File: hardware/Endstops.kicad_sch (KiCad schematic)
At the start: 47 parts

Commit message: Convert SCH files to latest version. Fix DRC Warnings in PrntrBoard.
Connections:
- net ~ALARM1 renamed ~{ALARM1}
- net ~ST1_ALARM renamed ~{ST1_ALARM}
- net ~ST2_ALARM renamed ~{ST2_ALARM}
- net ~ST3_ALARM renamed ~{ST3_ALARM}
- net ~ST4_ALARM renamed ~{ST4_ALARM}
- net ~ST5_ALARM renamed ~{ST5_ALARM}
- net ~ST6_ALARM renamed ~{ST6_ALARM}
- net ~U_MIN renamed ~{U_MIN}
- net ~V_MIN renamed ~{V_MIN}
- net ~X_MAX renamed ~{X_MAX}
- net ~X_MIN renamed ~{X_MIN}
- net ~Y_MAX renamed ~{Y_MAX}
- net ~Y_MIN renamed ~{Y_MIN}
- net ~Z_MAX renamed ~{Z_MAX}
- net ~Z_MIN renamed ~{Z_MIN}

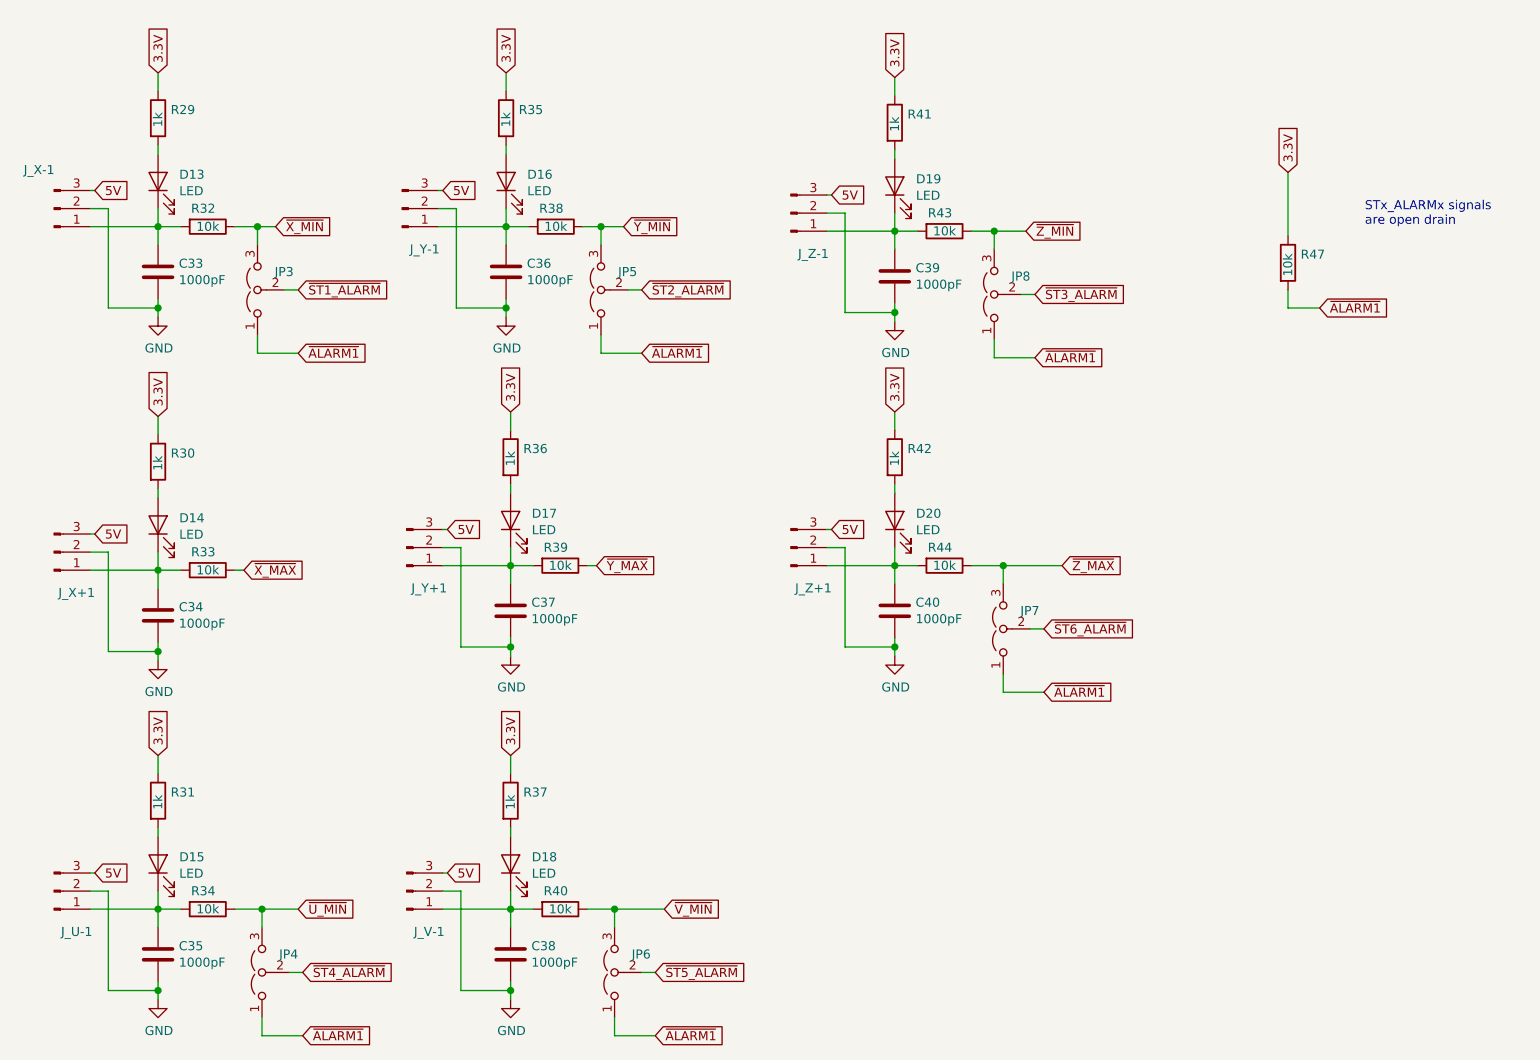
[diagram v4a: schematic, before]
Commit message: Add voltage selection for each stepper driver.
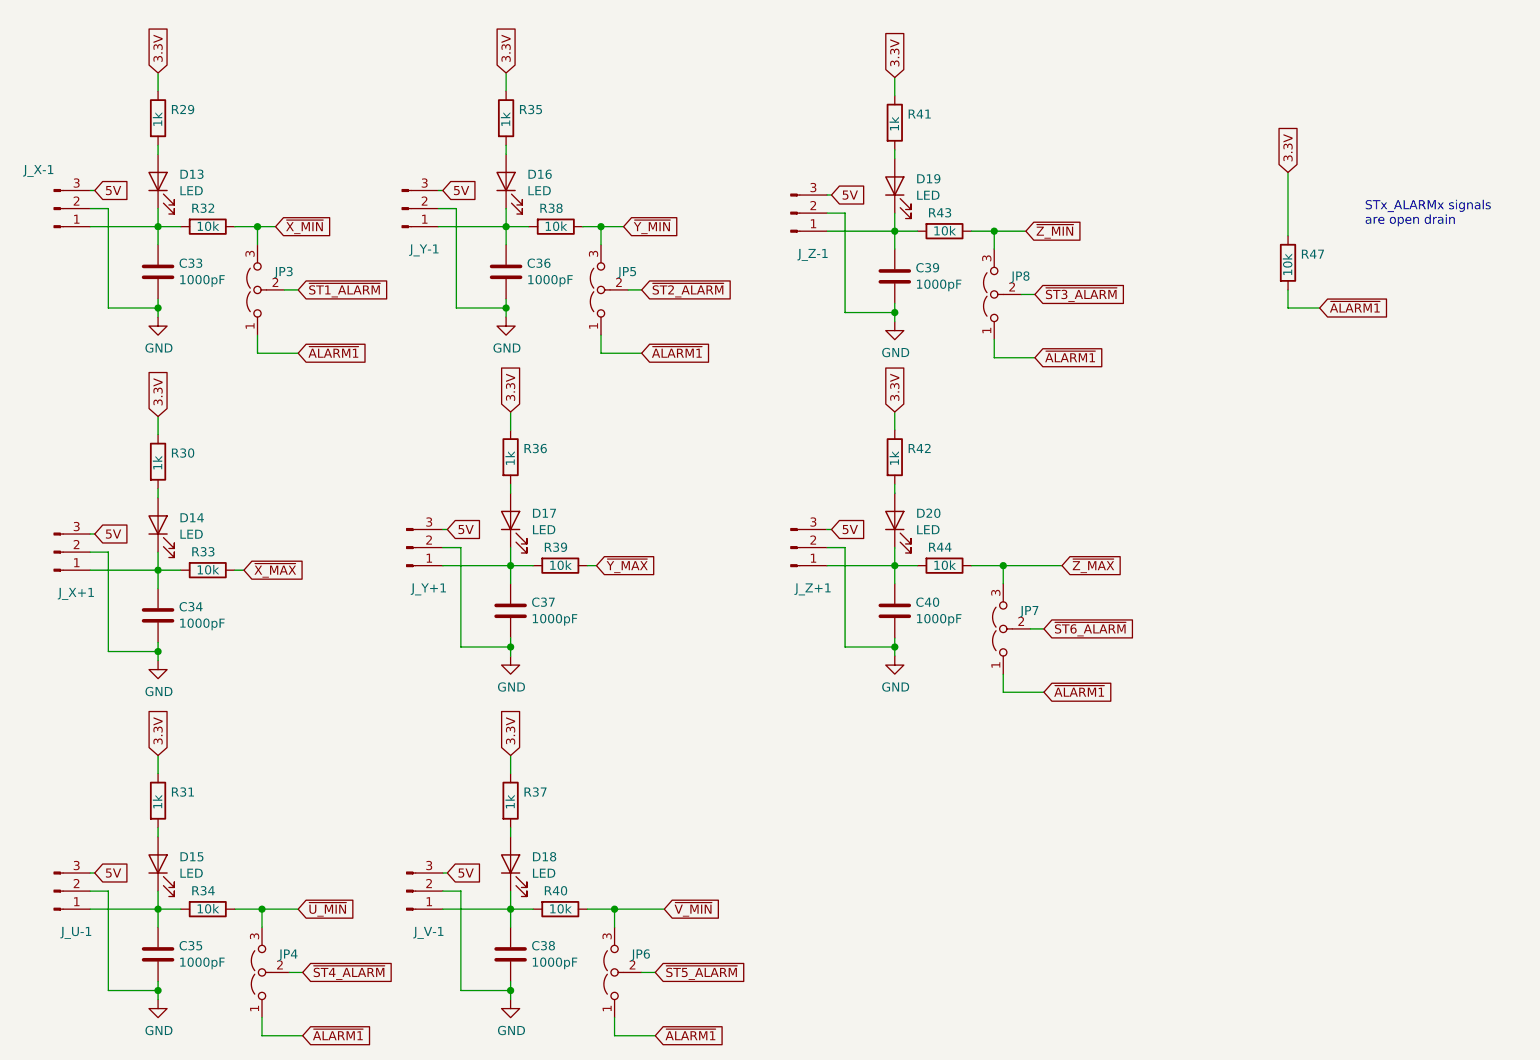
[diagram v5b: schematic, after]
